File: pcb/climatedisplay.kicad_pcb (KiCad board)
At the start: 2 copper layers, 100 x 100 mm, 66 parts, among them J1 Serial, J2 USB-C 6-Pin, SW1 RESET, SW2 FLASH, U1 ESP-12F, U10 2281AS, U11 2281AS, U12 2281AS, U13 MAX7219, U14 2281AS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

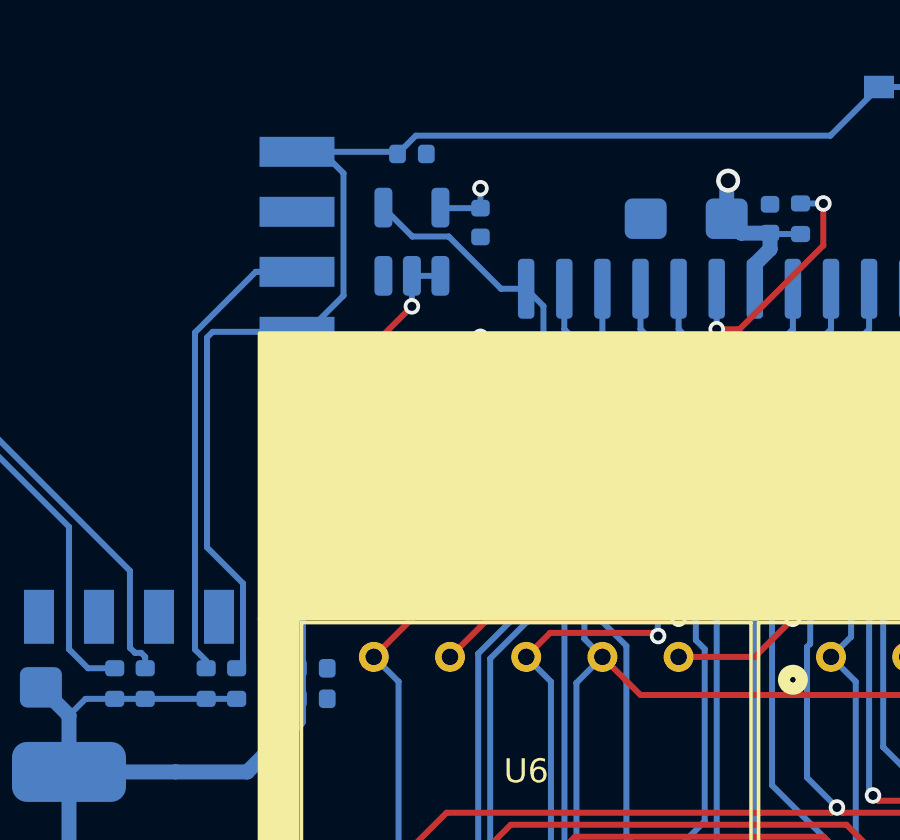
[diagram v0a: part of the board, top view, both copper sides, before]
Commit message: fix: footprints U2-U4
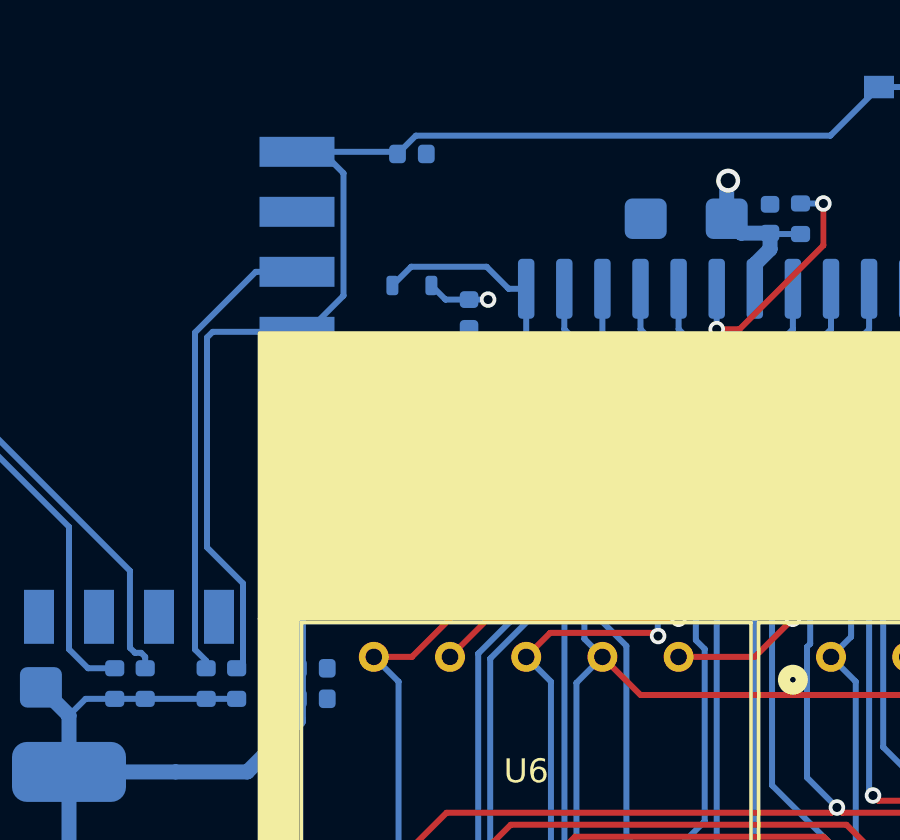
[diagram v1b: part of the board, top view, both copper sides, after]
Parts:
- U2, U3, U4: footprint Package_TO_SOT_SMD:SOT-23-5 -> Package_TO_SOT_SMD:SOT-353_SC-70-5
- moved C6 3.07 mm to (133.0, 58.5)
- moved U3 2.41 mm to (131.1, 58.5)
- moved C5 1.94 mm to (133.0, 62.3)
- moved U2 1.27 mm to (131.1, 62.3)
- moved C7 0.74 mm to (133.0, 66.1)
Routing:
- net /LOAD5V: track 129.0 -> 127.1 mm
- net /CLK: track 7.52 -> 6.11 mm
- net /LOAD: track 7.15 -> 6.29 mm
- net /CLK5V: track 128.8 -> 128.0 mm
